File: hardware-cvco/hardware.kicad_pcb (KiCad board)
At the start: 4 copper layers, 181 parts, among them J1 SMA, J2 SMA, J3 SMA, J4 SMA, J5 SMA, J6 SMA, J7 SMA, J9 DC, Q1 AOD403, Q2 PN2222A, SW1 On/Off, U1 L78L05_SOT89, U10 L78L05_SOT89, U11 L78L08_SOT89, U12 L78L10_SOT89, U13 PIC12F675-ISN, U14 NLB-310-T1, U15 NLB-310-T1, U16 NLB-310-T1, U18 LM317DCYR, U19 MCP73871-2AA, U20 TPS61046, U3 L78L12_SOT89, U4 L78L12_SOT89, U5 L78L10_SOT89, U6 NLB-310-T1, U7 NLB-310-T1, U8 NLB-310-T1, U9 NLB-310-T1, Y1 CVCO55CW-0100-0200, Y2 CVCO55CW-0200-0500, Y3 CV55CW500-1000, Y4 CVCO55CW-1000-2000, Y5 CV55BE1600-3200, Y6 CVCO55CC-3180-3710, Y7 CVCO55CW-3500-4500

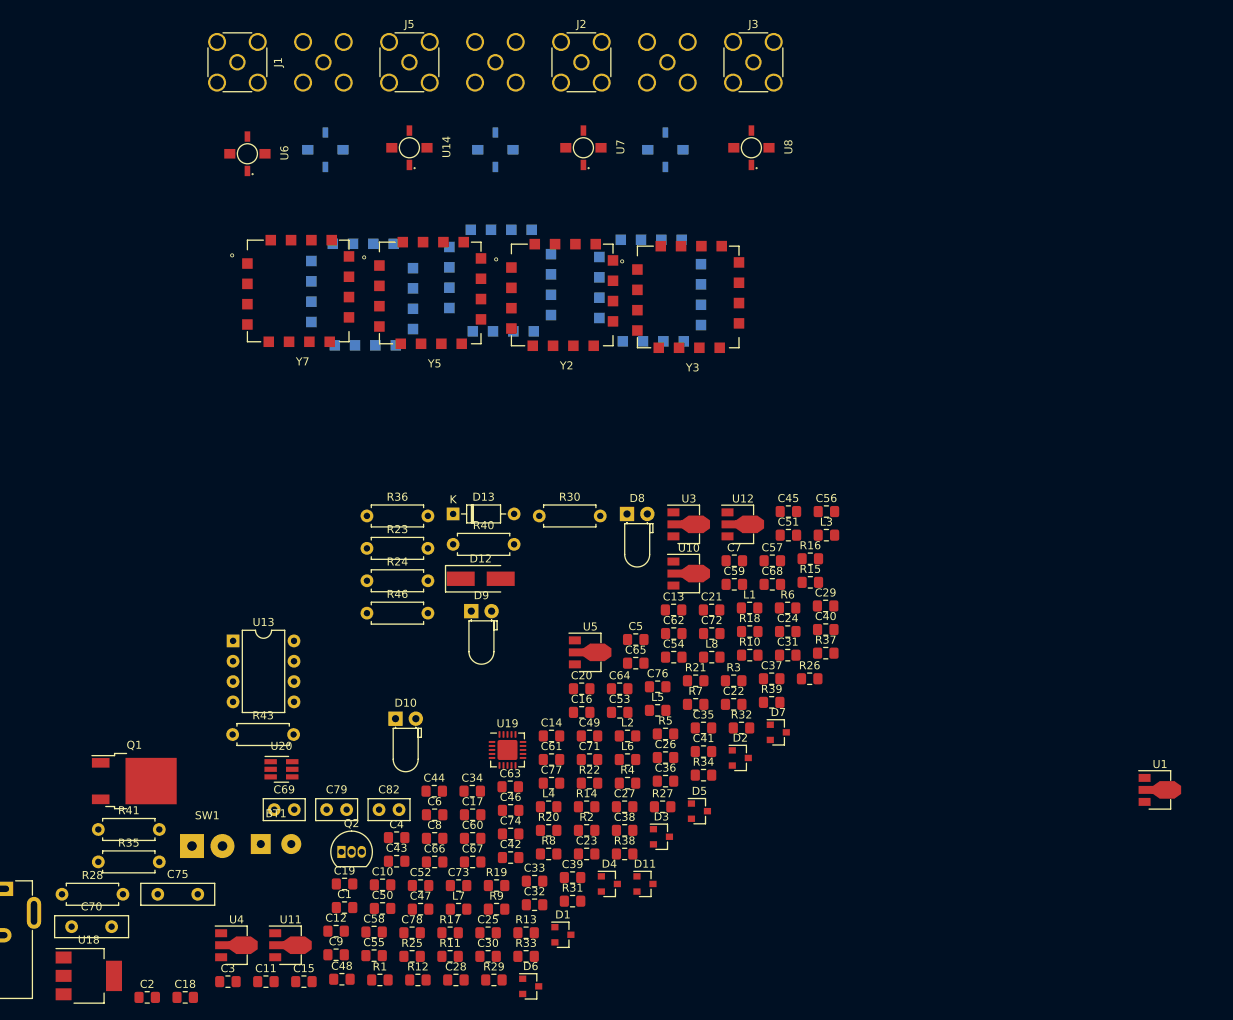
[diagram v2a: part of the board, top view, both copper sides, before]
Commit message: LCSC part numbers assigned.
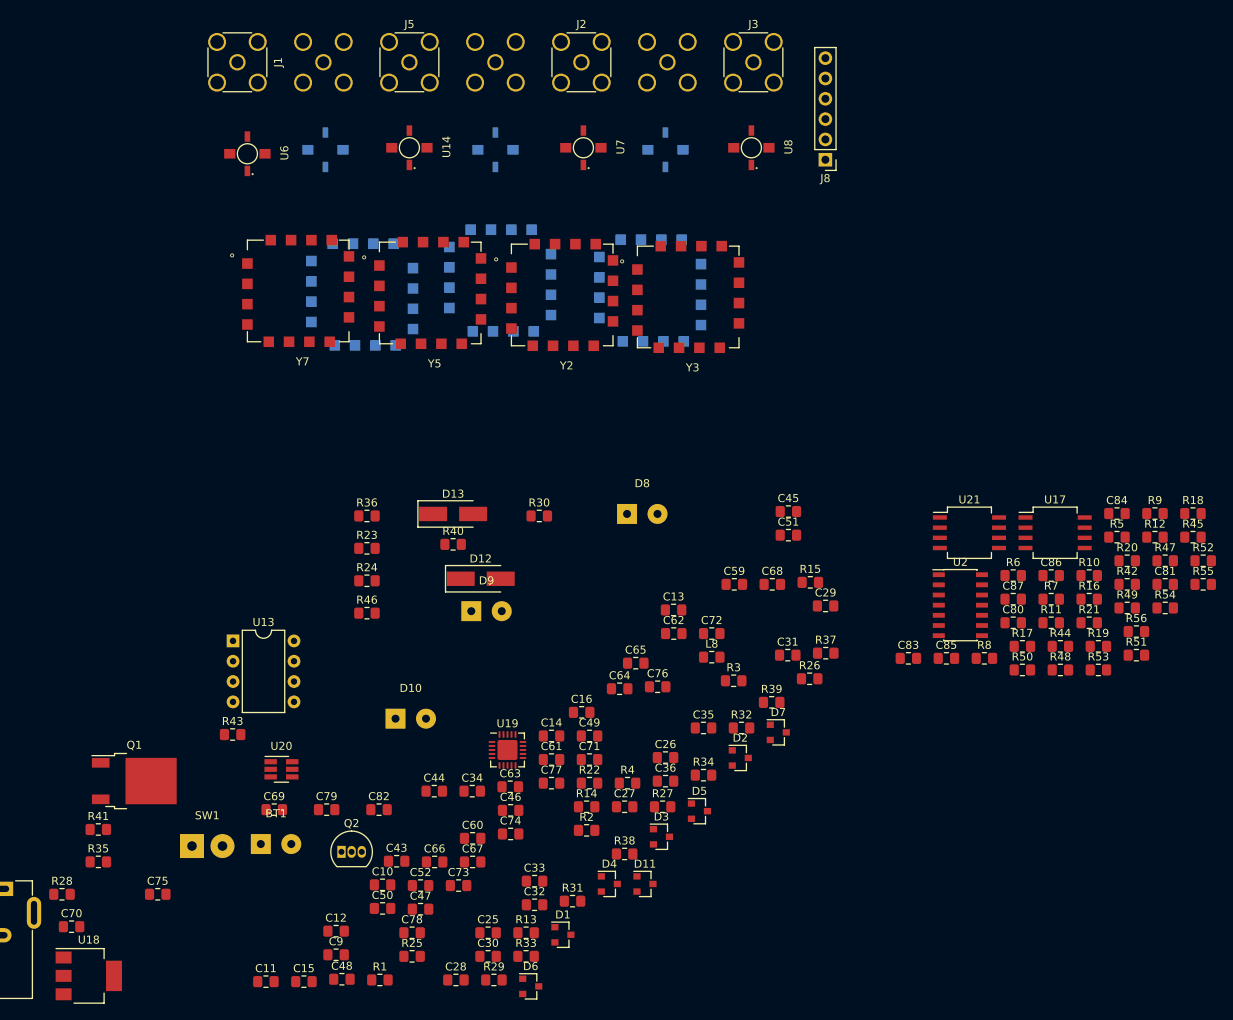
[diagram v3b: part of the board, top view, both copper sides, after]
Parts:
- removed C1, C3, C37, C39, C41, C5, C7: 1μ, Capacitor_SMD:C_0805_2012Metric_Pad1.15x1.40mm_HandSolder
- removed C17, C19, C21, C23, C53, C55, C57: 0.1n, Capacitor_SMD:C_0805_2012Metric_Pad1.15x1.40mm_HandSolder
- removed C18, C20, C22, C24, C54, C56, C58: 1n, Capacitor_SMD:C_0805_2012Metric_Pad1.15x1.40mm_HandSolder
- removed C2, C38, C4, C40, C42, C6, C8: 0.1u, Capacitor_SMD:C_0805_2012Metric_Pad1.15x1.40mm_HandSolder
- removed L1, L2, L3, L4, L5, L6, L7: 470n, Inductor_SMD:L_0805_2012Metric_Pad1.15x1.40mm_HandSolder
- removed U1, U10: L78L05_SOT89, Package_TO_SOT_SMD:SOT-89-3
- removed U11: L78L08_SOT89, Package_TO_SOT_SMD:SOT-89-3
- removed U12, U5: L78L10_SOT89, Package_TO_SOT_SMD:SOT-89-3
- removed U3, U4: L78L12_SOT89, Package_TO_SOT_SMD:SOT-89-3
- added C80: 0.1μF, Capacitor_SMD:C_0805_2012Metric_Pad1.15x1.40mm_HandSolder, F.Cu at (169.7, 130.6)
- added C81: 0.1μF, Capacitor_SMD:C_0805_2012Metric_Pad1.15x1.40mm_HandSolder, F.Cu at (188.7, 125.8)
- added C83: 0.1μF, Capacitor_SMD:C_0805_2012Metric_Pad1.15x1.40mm_HandSolder, F.Cu at (156.6, 135.1)
- added C84: 50pF, Capacitor_SMD:C_0805_2012Metric_Pad1.15x1.40mm_HandSolder, F.Cu at (182.7, 117.0)
- added C85: 10μF, Capacitor_SMD:C_0805_2012Metric_Pad1.15x1.40mm_HandSolder, F.Cu at (161.4, 135.1)
- added C86: 1nF, Capacitor_SMD:C_0805_2012Metric_Pad1.15x1.40mm_HandSolder, F.Cu at (174.5, 124.7)
- added C87: 10μF, Capacitor_SMD:C_0805_2012Metric_Pad1.15x1.40mm_HandSolder, F.Cu at (169.7, 127.7)
- added J8: Pickit 2, Connector_PinHeader_2.54mm:PinHeader_1x06_P2.54mm_Vertical, F.Cu at (146.2, 72.8)
- added R42: 1k, Resistor_SMD:R_0805_2012Metric_Pad1.15x1.40mm_HandSolder, F.Cu at (184.0, 125.8)
- added R44: 2k, Resistor_SMD:R_0805_2012Metric_Pad1.15x1.40mm_HandSolder, F.Cu at (175.6, 133.6)
- added R45: 3.3k, Resistor_SMD:R_0805_2012Metric_Pad1.15x1.40mm_HandSolder, F.Cu at (192.2, 119.9)
- added R47: 27k, Resistor_SMD:R_0805_2012Metric_Pad1.15x1.40mm_HandSolder, F.Cu at (188.7, 122.9)
- added R48: 6.7k, Resistor_SMD:R_0805_2012Metric_Pad1.15x1.40mm_HandSolder, F.Cu at (175.6, 136.5)
- added R49: 10, Resistor_SMD:R_0805_2012Metric_Pad1.15x1.40mm_HandSolder, F.Cu at (184.0, 128.8)
- added R50: 1k, Resistor_SMD:R_0805_2012Metric_Pad1.15x1.40mm_HandSolder, F.Cu at (170.9, 136.5)
- added R51: 3.9k, Resistor_SMD:R_0805_2012Metric_Pad1.15x1.40mm_HandSolder, F.Cu at (185.1, 134.7)
- added R52: 2k, Resistor_SMD:R_0805_2012Metric_Pad1.15x1.40mm_HandSolder, F.Cu at (193.5, 122.9)
- added R53: 1.4k, Resistor_SMD:R_0805_2012Metric_Pad1.15x1.40mm_HandSolder, F.Cu at (180.4, 136.5)
- added R54: 1k, Resistor_SMD:R_0805_2012Metric_Pad1.15x1.40mm_HandSolder, F.Cu at (188.7, 128.8)
- added R55: 1k, Resistor_SMD:R_0805_2012Metric_Pad1.15x1.40mm_HandSolder, F.Cu at (193.5, 125.8)
- added R56: 1k, Resistor_SMD:R_0805_2012Metric_Pad1.15x1.40mm_HandSolder, F.Cu at (185.1, 131.7)
- added U17: LM358, Package_SO:SO-8_5.3x6.2mm_P1.27mm, F.Cu at (175.0, 119.4)
- added U2: 74LS07, Package_SO:SOIC-14_3.9x8.7mm_P1.27mm, F.Cu at (163.1, 128.4)
- added U21: LM386, Package_SO:SO-8_5.3x6.2mm_P1.27mm, F.Cu at (164.3, 119.4)
- C10, C12, C14, C16, C30, C32, C34, C36, C48, C50, C52, C63, C65, C67: value 0.1n -> 0.1nF
- C11, C13, C15, C29, C31, C33, C35, C47, C49, C51, C62, C64, C66, C9: value 1n -> 1nF
- C69, C79, C82: footprint Capacitor_THT:C_Disc_D5.0mm_W2.5mm_P2.50mm -> Capacitor_SMD:C_0805_2012Metric_Pad1.15x1.40mm_HandSolder
- C70, C75: footprint Capacitor_THT:C_Disc_D9.0mm_W2.5mm_P5.00mm -> Capacitor_SMD:C_0805_2012Metric_Pad1.15x1.40mm_HandSolder
- D10, D8, D9: footprint LED_THT:LED_D3.0mm_Horizontal_O1.27mm_Z2.0mm -> Connector_Wire:SolderWirePad_1x02_P3.81mm_Drill1mm
- D13: footprint Diode_THT:D_DO-35_SOD27_P7.62mm_Horizontal -> Diode_SMD:D_SMA_Handsoldering
- R10: value 560 -> 1k
- R11: value 680 -> 1k
- R12: value 470 -> 1.4k
- R16, R5: value 82 -> 220
- R17: value 120 -> 270
- R18, R8: value 150 -> 470
- R19: value 220 -> 1k
- R20: value 270 -> 1k
- R21: value 470 -> 1k
- R23, R24, R28, R30, R35, R36, R40, R41, R43, R46: footprint Resistor_THT:R_Axial_DIN0207_L6.3mm_D2.5mm_P7.62mm_Horizontal -> Resistor_SMD:R_0805_2012Metric_Pad1.15x1.40mm_HandSolder
- R6: value 180 -> 560
- R7: value 180 -> 680
- R9: value 220 -> 3.9k
- moved R12 107.5 mm to (187.4, 119.9)
- moved R9 96.0 mm to (187.4, 117.0)
- moved R11 85.9 mm to (174.5, 130.6)
- moved R19 81.0 mm to (180.4, 133.6)
- moved R17 80.0 mm to (170.9, 133.6)
- moved R20 79.8 mm to (184.0, 122.9)
- moved R5 61.6 mm to (182.7, 119.9)
- moved R8 59.7 mm to (166.1, 135.1)
- moved R18 57.3 mm to (192.2, 117.0)
- moved R21 49.7 mm to (179.2, 130.6)
- moved R7 46.3 mm to (174.5, 127.7)
- moved R10 43.6 mm to (179.2, 124.7)
- moved R16 35.2 mm to (179.2, 127.7)
- moved R6 28.5 mm to (169.7, 124.7)
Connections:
- C10 pad 1: VCC_1 -> Net-(C10-Pad1)
- C11 pad 1: VCC_2 -> Net-(C11-Pad1)
- C12 pad 1: VCC_2 -> Net-(C11-Pad1)
- C13 pad 1: VCC_3 -> Net-(C13-Pad1)
- C14 pad 1: VCC_3 -> Net-(C13-Pad1)
- C15 pad 1: VCC_4 -> Net-(C15-Pad1)
- C16 pad 1: VCC_4 -> Net-(C15-Pad1)
- C47 pad 1: VCC_5 -> Net-(C47-Pad1)
- C48 pad 1: VCC_5 -> Net-(C47-Pad1)
- C49 pad 1: VCC_6 -> Net-(C49-Pad1)
- C50 pad 1: VCC_6 -> Net-(C49-Pad1)
- C51 pad 1: VCC_7 -> Net-(C51-Pad1)
- C52 pad 1: VCC_7 -> Net-(C51-Pad1)
- C9 pad 1: VCC_1 -> Net-(C10-Pad1)
- J1 pad 1: Net-(J1-Pad1) -> P2_VSS
- J2 pad 1: Net-(J2-Pad1) -> P2_VSS
- J3 pad 1: Net-(J3-Pad1) -> P2_VSS
- J4 pad 1: Net-(J4-Pad1) -> P2_VSS
- J5 pad 1: Net-(J5-Pad1) -> P2_VSS
- J6 pad 1: Net-(J6-Pad1) -> P2_VSS
- J7 pad 1: Net-(J7-Pad1) -> P2_VSS
- R10 pad 1: P2_VSS -> VCC_2
- R10 pad 2: Net-(R10-Pad2) -> P2_VDD
- R11 pad 1: P2_VSS -> VCC_3
- R11 pad 2: Net-(R11-Pad2) -> P2_VDD
- R12 pad 1: P2_VSS -> VCC_4
- R12 pad 2: Net-(R12-Pad2) -> P2_VDD
- R16 pad 1: VCC_5 -> Net-(C47-Pad1)
- R16 pad 2: Net-(L5-Pad1) -> VCC_5
- R17 pad 1: VCC_6 -> Net-(C49-Pad1)
- R17 pad 2: Net-(L6-Pad1) -> VCC_6
- R18 pad 1: VCC_7 -> Net-(C51-Pad1)
- R18 pad 2: Net-(L7-Pad1) -> VCC_7
- R19 pad 1: P2_VSS -> VCC_1
- R19 pad 2: Net-(R19-Pad2) -> P2_VSS
- R20 pad 1: P2_VSS -> VCC_2
- R20 pad 2: Net-(R20-Pad2) -> P2_VSS
- R21 pad 1: P2_VSS -> VCC_3
- R21 pad 2: Net-(R21-Pad2) -> P2_VSS
- R5 pad 1: VCC_1 -> Net-(C10-Pad1)
- R5 pad 2: Net-(L1-Pad1) -> VCC_1
- R6 pad 1: VCC_2 -> Net-(C11-Pad1)
- R6 pad 2: Net-(L2-Pad1) -> VCC_2
- R7 pad 1: VCC_3 -> Net-(C13-Pad1)
- R7 pad 2: Net-(L3-Pad1) -> VCC_3
- R8 pad 1: VCC_4 -> Net-(C15-Pad1)
- R8 pad 2: Net-(L4-Pad1) -> VCC_4
- R9 pad 1: P2_VSS -> VCC_1
- R9 pad 2: Net-(R9-Pad2) -> P2_VDD
- U14 pad 3: Net-(J5-Pad1) -> P2_VSS
- U15 pad 3: Net-(J6-Pad1) -> P2_VSS
- U16 pad 3: Net-(J7-Pad1) -> P2_VSS
- U6 pad 3: Net-(J1-Pad1) -> P2_VSS
- U7 pad 3: Net-(J2-Pad1) -> P2_VSS
- U8 pad 3: Net-(J3-Pad1) -> P2_VSS
- U9 pad 3: Net-(J4-Pad1) -> P2_VSS
- Y1 pad 14: Net-(R9-Pad2) -> P2_VSS
- Y2 pad 14: Net-(R10-Pad2) -> P2_VSS
- Y3 pad 14: Net-(R11-Pad2) -> P2_VSS
- Y4 pad 14: Net-(R12-Pad2) -> P2_VSS
- Y5 pad 14: Net-(R19-Pad2) -> P2_VSS
- Y6 pad 14: Net-(R20-Pad2) -> P2_VSS
- Y7 pad 14: Net-(R21-Pad2) -> P2_VSS

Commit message: RF layout - start.
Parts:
- C59, C60, C61, J5, U14, Y5, Y7: moved to B.Cu
- C70, C75: value 220nF -> 1μF
- J4, U9, Y1, Y4: moved to F.Cu
- J8: footprint Connector_PinHeader_2.54mm:PinHeader_1x06_P2.54mm_Vertical -> Connector_PinSocket_2.54mm:PinSocket_1x06_P2.54mm_Vertical
- moved U2 124.5 mm to (40.0, 110.0)
- moved C28 117.4 mm to (150.0, 69.0), turned to 270 degrees
- moved C25 103.2 mm to (80.0, 69.0), turned to 270 degrees
- moved C60 89.5 mm to (115.0, 69.0), turned to 270 degrees
- moved C27 84.8 mm to (126.7, 69.0), turned to 270 degrees
- moved U13 84.5 mm to (150.0, 100.0)
- moved C61 83.0 mm to (138.3, 69.0), turned to 270 degrees
- moved C26 81.8 mm to (103.3, 69.0), turned to 270 degrees
- moved C59 71.4 mm to (91.7, 69.0), turned to 270 degrees
- moved J9 67.2 mm to (75.0, 105.0)
- moved U9 66.8 mm to (150.0, 63.0), turned to 90 degrees
- moved J4 66.8 mm to (150.0, 54.5), turned to 0 degrees
- moved Y7 66.3 mm to (136.3, 72.9)
- moved Y4 54.1 mm to (153.3, 85.0), turned to 90 degrees
- moved D13 49.0 mm to (52.5, 130.0)
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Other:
- board outline added: 100 x 70 mm
